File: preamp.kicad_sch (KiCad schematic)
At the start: 11 parts, among them U2 OPA357AIDBVR, U7 LM4040AIM3-3.0+T

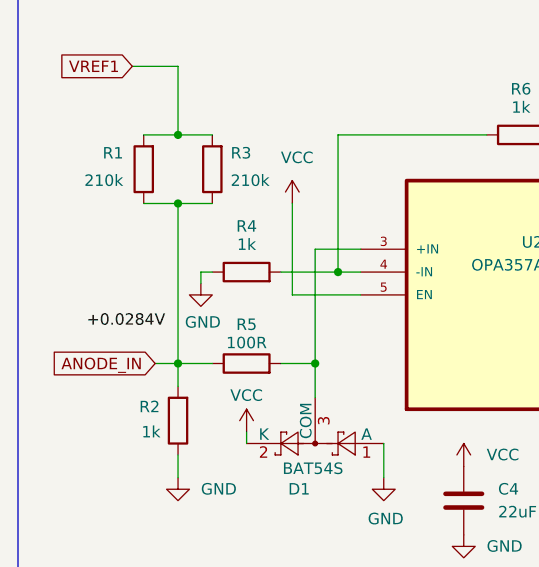
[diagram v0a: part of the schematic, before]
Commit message: ERC errors fix
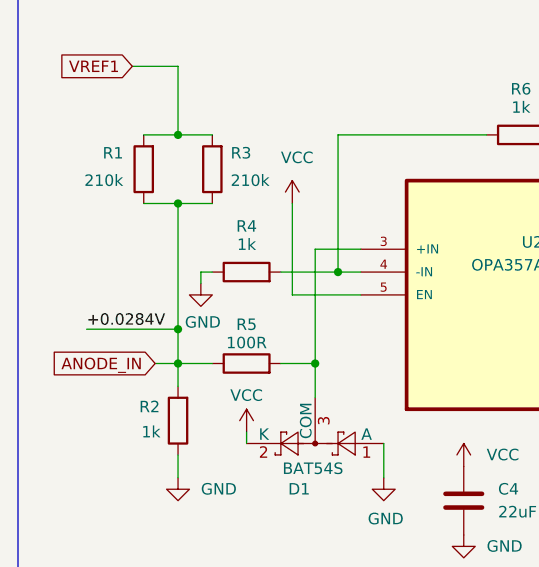
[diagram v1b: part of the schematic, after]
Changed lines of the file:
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@@
+	)
+	(junction
+		(at 72.39 90.17)
+		(diameter 0)
+		(color 0 0 0 0)
 	)
 	(junction
@@
 	(wire
 		(pts
+			(xy 72.39 90.17) (xy 72.39 93.98)
+		)
+		(stroke
+			(width 0)
+			(type default)
+		)
+	)
+	(wire
+		(pts
 			(xy 67.31 142.24) (xy 73.66 142.24)
 		)
@@
 	(wire
 		(pts
+			(xy 62.23 90.17) (xy 72.39 90.17)
+		)
+		(stroke
+			(width 0)
+			(type default)
+		)
+	)
+	(wire
+		(pts
 			(xy 68.58 68.58) (xy 72.39 68.58)
 		)
@@
 	(wire
 		(pts
-			(xy 72.39 76.2) (xy 72.39 93.98)
-		)
-		(stroke
+			(xy 72.39 76.2) (xy 72.39 90.17)
+		)
+		(stroke

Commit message: ERC test
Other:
- moved on the sheet: C4, C5, D1, R1, R2, R3, R4, R5, R6, U2, U7
